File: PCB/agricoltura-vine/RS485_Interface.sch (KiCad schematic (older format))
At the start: 10 parts

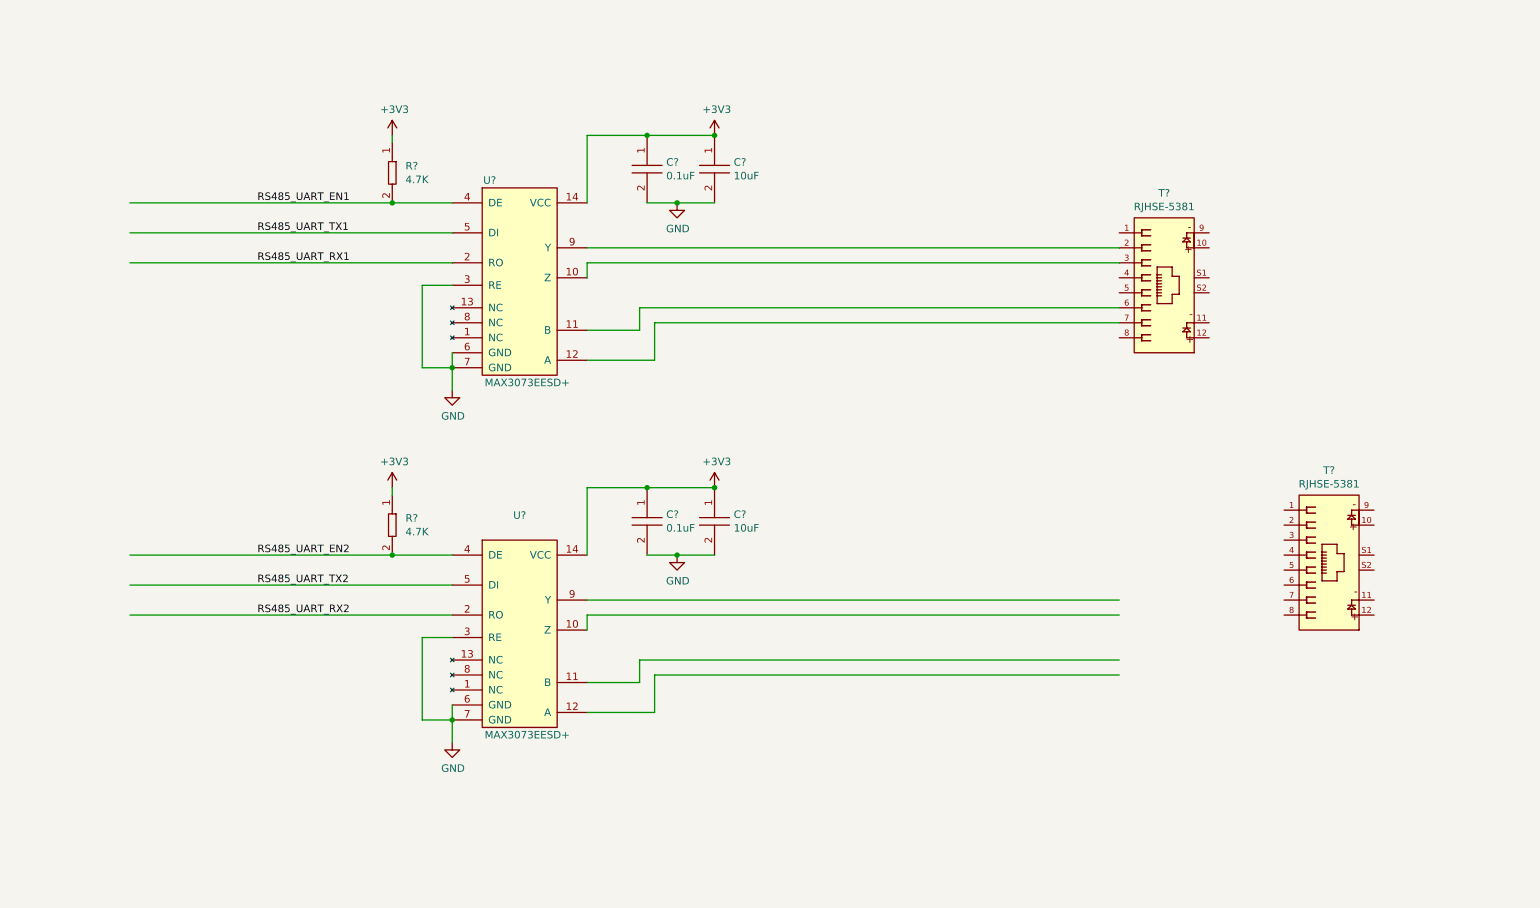
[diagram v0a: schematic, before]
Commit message: Schematic process
scheamtics laid out for all board subsyhstems, connecting MCU to subsystems still in progress, power yet to be designed.
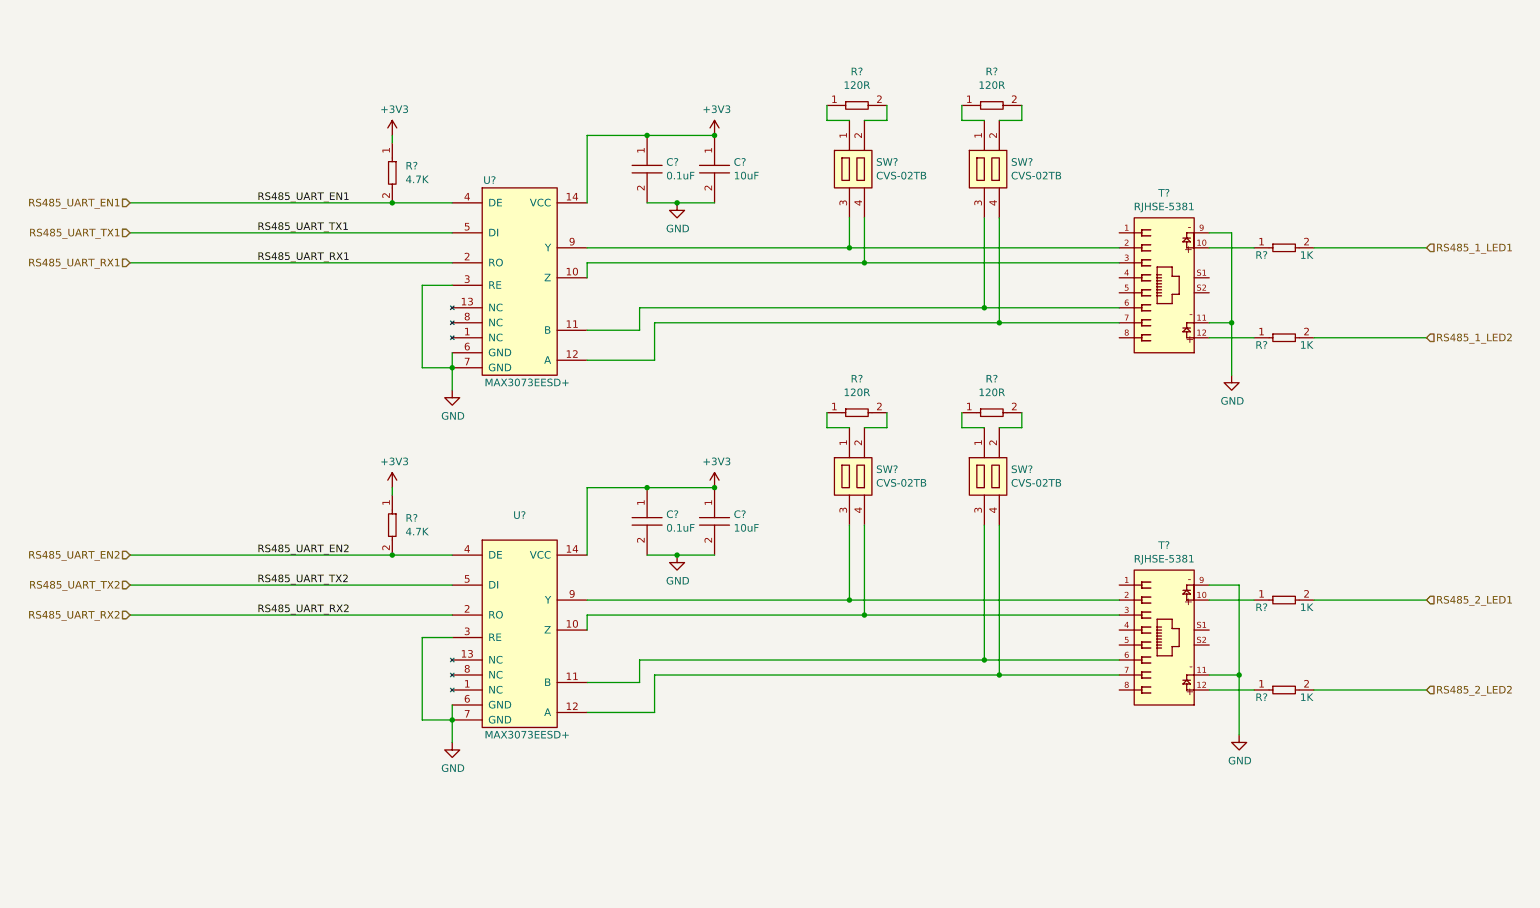
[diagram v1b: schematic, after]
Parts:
- added R? (x4): AC0402FR-07120RL, AVR-KiCAD-Lib-Resistors:R0402, symbol AVR-KiCAD-Lib-Resistors:AC0402FR-07120RL
- added R? (x4): RC0402FR-071KL, AVR-KiCAD-Lib-Resistors:R0402, symbol AVR-KiCAD-Lib-Resistors:RC0402FR-071KL
- added SW? (x4): CVS-02TB, AVR-KiCAD-Lib-Mech-Switches:CVS-02TB, symbol AVR-KiCAD-Lib-Mech-Switches:CVS-02TB
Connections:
- net labels added: RS485_1_LED1, RS485_1_LED2, RS485_2_LED1, RS485_2_LED2
- wire segments 48 -> 96
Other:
- moved on the sheet: T?

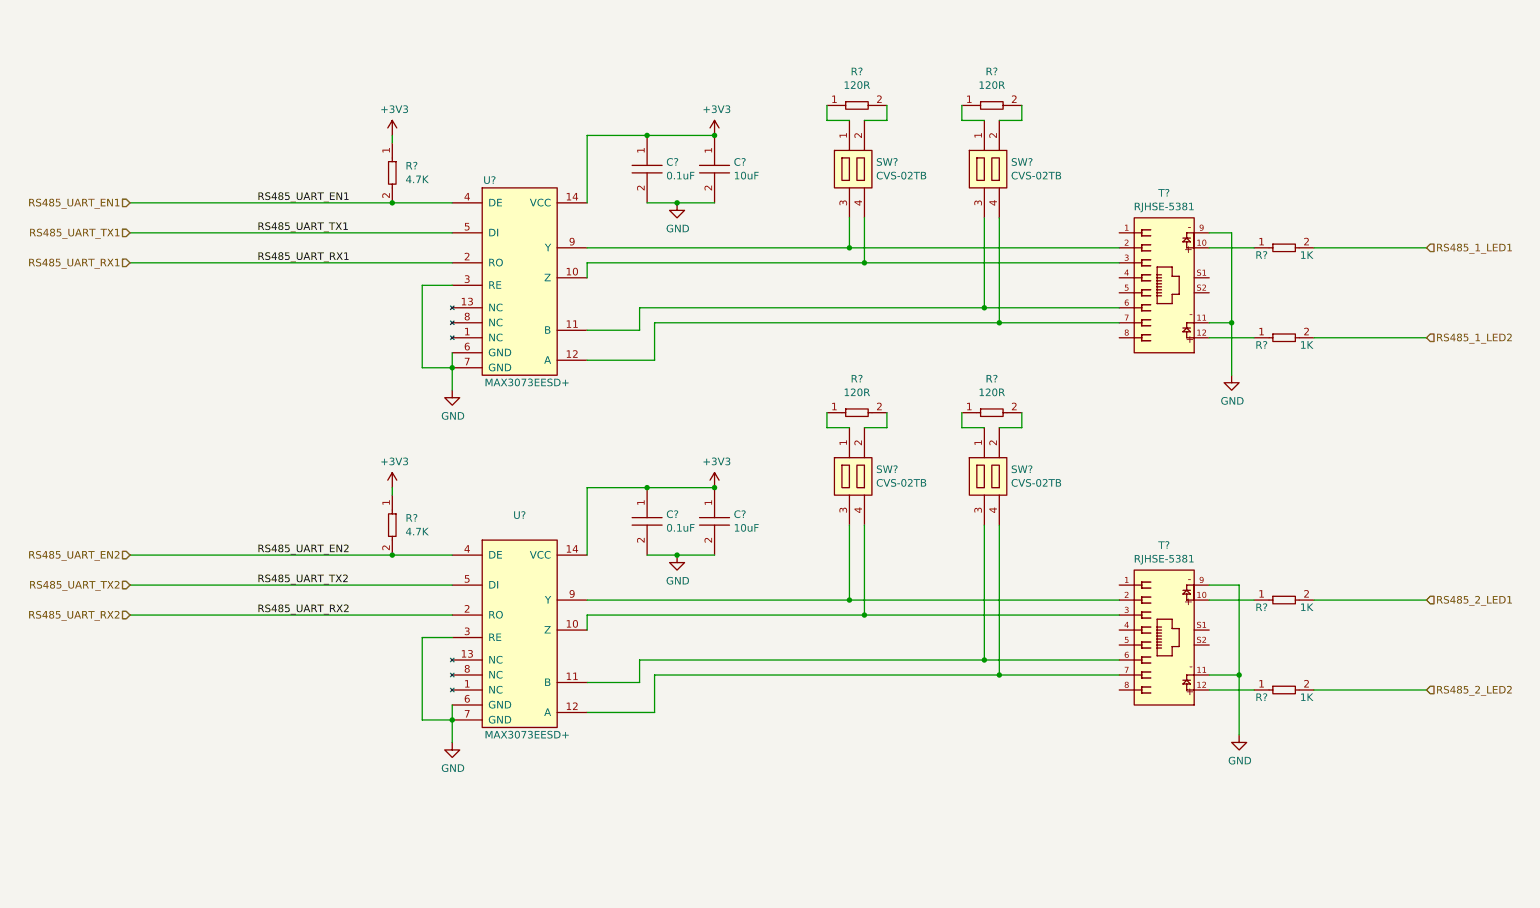
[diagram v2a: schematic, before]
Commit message: Board
Board shape defined, though subject to change. Schematic anotated and parts exported to board.
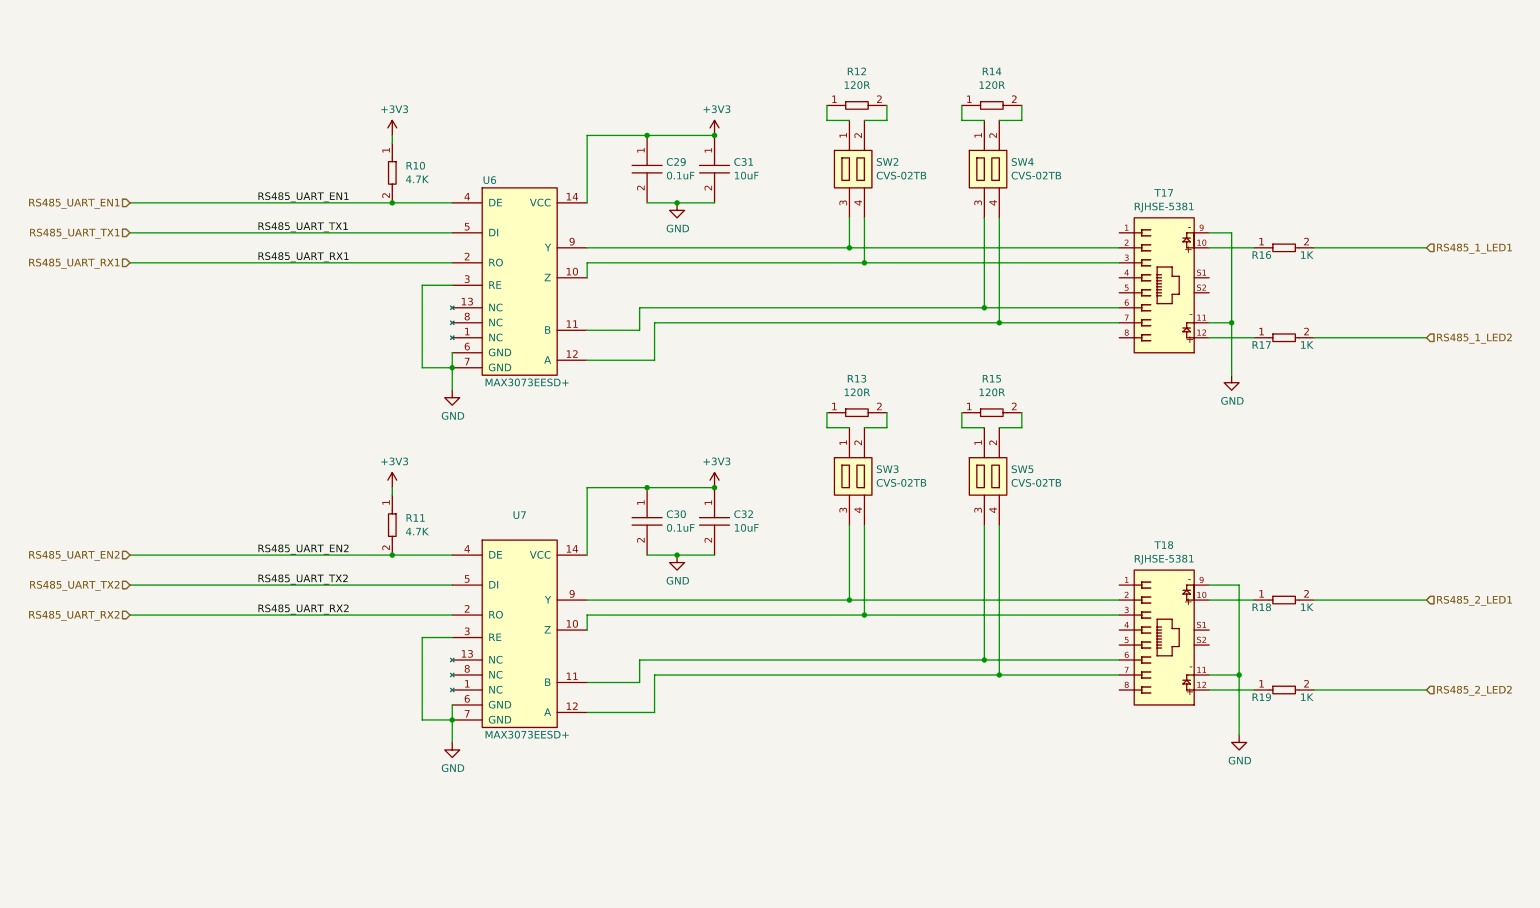
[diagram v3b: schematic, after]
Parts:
- gave numbers to parts that had none: 22
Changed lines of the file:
@@
 $EndDescr
 $Comp
-L AVR-KiCAD-Lib-ICs:MAX3073EESD+ U?
+L AVR-KiCAD-Lib-ICs:MAX3073EESD+ U6
 U 1 1 5EFD4AB7
 P 4300 2150
-F 0 "U?" H 4350 2250 50  0000 C CNN
+F 0 "U6" H 4350 2250 50  0000 C CNN
 F 1 "MAX3073EESD+" H 4350 2350 50  0001 C CNN
 F 2 "AVR-KiCAD-Lib-ICs:MAX3073EESD&plus_" H 4100 2150 50  0001 C CNN
@@
 $EndComp
 $Comp
-L AVR-KiCAD-Lib-ICs:MAX3073EESD+ U?
+L AVR-KiCAD-Lib-ICs:MAX3073EESD+ U7
 U 1 1 5EFD5614
 P 4300 4500
-F 0 "U?" H 4550 4715 50  0000 C CNN
+F 0 "U7" H 4550 4715 50  0000 C CNN
 F 1 "MAX3073EESD+" H 4350 4700 50  0001 C CNN
 F 2 "AVR-KiCAD-Lib-ICs:MAX3073EESD&plus_" H 4100 4500 50  0001 C CNN
@@
 $EndComp
 $Comp
-L AVR-KiCAD-Lib-Connectors:RJHSE-5381 T?
+L AVR-KiCAD-Lib-Connectors:RJHSE-5381 T17
 U 1 1 5EFFC7BA
 P 9050 2300
-F 0 "T?" H 9250 2465 50  0000 C CNN
+F 0 "T17" H 9250 2465 50  0000 C CNN
 F 1 "RJHSE-5381" H 9250 2374 50  0000 C CNN
 F 2 "AVR-KiCAD-Lib-Connectors:AMPHENOL_RJHSE-5381" H 8850 2300 50  0001 C CNN
@@
 $EndComp
 $Comp
-L AVR-KiCAD-Lib-Connectors:RJHSE-5381 T?
+L AVR-KiCAD-Lib-Connectors:RJHSE-5381 T18
 U 1 1 5EFFF009
 P 9050 4650
-F 0 "T?" H 9250 4815 50  0000 C CNN
+F 0 "T18" H 9250 4815 50  0000 C CNN
 F 1 "RJHSE-5381" H 9250 4724 50  0000 C CNN
 F 2 "AVR-KiCAD-Lib-Connectors:AMPHENOL_RJHSE-5381" H 8850 4650 50  0001 C CNN
@@
 	5450 3000 7750 3000
 $Comp
-L power:GND #PWR?
+L power:GND #PWR044
 U 1 1 5F017F66
 P 5600 2200
-F 0 "#PWR?" H 5600 1950 50  0001 C CNN
+F 0 "#PWR044" H 5600 1950 50  0001 C CNN
 F 1 "GND" H 5605 2027 50  0000 C CNN
 F 2 "" H 5600 2200 50  0001 C CNN
@@
 	5600 2200 5850 2200
 $Comp
-L power:GND #PWR?
+L power:GND #PWR042
 U 1 1 5F01B1E0
 P 4100 3450
-F 0 "#PWR?" H 4100 3200 50  0001 C CNN
+F 0 "#PWR042" H 4100 3200 50  0001 C CNN
 F 1 "GND" H 4105 3277 50  0000 C CNN
 F 2 "" H 4100 3450 50  0001 C CNN
@@
 	4100 3300 4100 3450
 $Comp
-L AVR-KiCAD-Lib-Resistors:RC0402FR-074K7L R?
+L AVR-KiCAD-Lib-Resistors:RC0402FR-074K7L R10
 U 1 1 5F01CC10
 P 3700 2000
-F 0 "R?" V 3654 2088 50  0000 L CNN
+F 0 "R10" V 3654 2088 50  0000 L CNN
 F 1 "RC0402FR-074K7L" V 3700 2087 50  0001 L CNN
 F 2 "AVR-KiCAD-Lib-Resistors:R0402" H 3700 2000 50  0001 C CNN
@@
 $EndComp
 $Comp
-L power:+3V3 #PWR?
+L power:+3V3 #PWR040
 U 1 1 5F01FD5B
 P 3700 1750
-F 0 "#PWR?" H 3700 1600 50  0001 C CNN
+F 0 "#PWR040" H 3700 1600 50  0001 C CNN
 F 1 "+3V3" H 3715 1923 50  0000 C CNN
 F 2 "" H 3700 1750 50  0001 C CNN
@@
 	5450 5350 7750 5350
 $Comp
-L AVR-KiCAD-Lib-Capacitors:C0402C104K9PACTU C?
+L AVR-KiCAD-Lib-Capacitors:C0402C104K9PACTU C30
 U 1 1 5F03829B
 P 5400 4300
-F 0 "C?" V 5379 4428 50  0000 L CNN
+F 0 "C30" V 5379 4428 50  0000 L CNN
 F 1 "C0402C104K9PACTU" H 5450 4500 50  0001 C CNN
 F 2 "AVR-KiCAD-Lib-Resistors:R0402" H 5200 4300 50  0001 C CNN
@@
 $EndComp
 $Comp
-L AVR-KiCAD-Lib-Capacitors:GRM188R61A106KE69J C?
+L AVR-KiCAD-Lib-Capacitors:GRM188R61A106KE69J C32
 U 1 1 5F0382BA
 P 5850 4300
-F 0 "C?" V 5829 4428 50  0000 L CNN
+F 0 "C32" V 5829 4428 50  0000 L CNN
 F 1 "GRM188R61A106KE69J" H 5900 4500 50  0001 C CNN
 F 2 "AVR-KiCAD-Lib-Capacitors:C0603" H 5650 4300 50  0001 C CNN
@@
 $EndComp
 $Comp
-L power:GND #PWR?
+L power:GND #PWR045
 U 1 1 5F0382C0
 P 5600 4550
-F 0 "#PWR?" H 5600 4300 50  0001 C CNN
+F 0 "#PWR045" H 5600 4300 50  0001 C CNN
 F 1 "GND" H 5605 4377 50  0000 C CNN
 F 2 "" H 5600 4550 50  0001 C CNN
@@
 	5600 4550 5850 4550
 $Comp
-L power:+3V3 #PWR?
+L power:+3V3 #PWR047
 U 1 1 5F0382CD
 P 5850 4100
-F 0 "#PWR?" H 5850 3950 50  0001 C CNN
+F 0 "#PWR047" H 5850 3950 50  0001 C CNN
 F 1 "+3V3" H 5865 4273 50  0000 C CNN
 F 2 "" H 5850 4100 50  0001 C CNN
@@
 Connection ~ 5850 4100
 $Comp
-L power:GND #PWR?
+L power:GND #PWR043
 U 1 1 5F0382D4
 P 4100 5800
-F 0 "#PWR?" H 4100 5550 50  0001 C CNN
+F 0 "#PWR043" H 4100 5550 50  0001 C CNN
 F 1 "GND" H 4105 5627 50  0000 C CNN
 F 2 "" H 4100 5800 50  0001 C CNN
@@
 	4100 5650 4100 5800
 $Comp
-L AVR-KiCAD-Lib-Resistors:RC0402FR-074K7L R?
+L AVR-KiCAD-Lib-Resistors:RC0402FR-074K7L R11
 U 1 1 5F0382F6
 P 3700 4350
-F 0 "R?" V 3654 4438 50  0000 L CNN
+F 0 "R11" V 3654 4438 50  0000 L CNN
 F 1 "RC0402FR-074K7L" V 3700 4437 50  0001 L CNN
 F 2 "AVR-KiCAD-Lib-Resistors:R0402" H 3700 4350 50  0001 C CNN
@@
 $EndComp
 $Comp
-L power:+3V3 #PWR?
+L power:+3V3 #PWR041
 U 1 1 5F0382FC
 P 3700 4100
-F 0 "#PWR?" H 3700 3950 50  0001 C CNN
+F 0 "#PWR041" H 3700 3950 50  0001 C CNN
 F 1 "+3V3" H 3715 4273 50  0000 C CNN
 F 2 "" H 3700 4100 50  0001 C CNN
@@
 RS485_UART_EN2
 $Comp
-L AVR-KiCAD-Lib-Resistors:AC0402FR-07120RL R?
+L AVR-KiCAD-Lib-Resistors:AC0402FR-07120RL R12
 U 1 1 5F099D8E
 P 6800 1550
-F 0 "R?" H 6800 1775 50  0000 C CNN
+F 0 "R12" H 6800 1775 50  0000 C CNN
 F 1 "AC0402FR-07120RL" H 6800 1775 50  0001 C CNN
 F 2 "AVR-KiCAD-Lib-Resistors:R0402" H 6800 1550 50  0001 C CNN
@@
 $EndComp
 $Comp
-L AVR-KiCAD-Lib-Mech-Switches:CVS-02TB SW?
+L AVR-KiCAD-Lib-Mech-Switches:CVS-02TB SW2
 U 1 1 5F09CD45
 P 6700 1900
-F 0 "SW?" H 6928 1871 50  0000 L CNN
+F 0 "SW2" H 6928 1871 50  0000 L CNN
 F 1 "CVS-02TB" H 6928 1780 50  0000 L CNN
 F 2 "AVR-KiCAD-Lib-Mech-Switches:CVS-02TB" H 6700 2400 50  0001 C CNN
@@
 	6850 2600 5000 2600
 $Comp
-L AVR-KiCAD-Lib-Resistors:AC0402FR-07120RL R?
+L AVR-KiCAD-Lib-Resistors:AC0402FR-07120RL R14
 U 1 1 5F0B259F
 P 7700 1550
-F 0 "R?" H 7700 1775 50  0000 C CNN
+F 0 "R14" H 7700 1775 50  0000 C CNN
 F 1 "AC0402FR-07120RL" H 7700 1775 50  0001 C CNN
 F 2 "AVR-KiCAD-Lib-Resistors:R0402" H 7700 1550 50  0001 C CNN
@@
 $EndComp
 $Comp
-L AVR-KiCAD-Lib-Mech-Switches:CVS-02TB SW?
+L AVR-KiCAD-Lib-Mech-Switches:CVS-02TB SW4
 U 1 1 5F0B25BE
 P 7600 1900
-F 0 "SW?" H 7828 1871 50  0000 L CNN
+F 0 "SW4" H 7828 1871 50  0000 L CNN
 F 1 "CVS-02TB" H 7828 1780 50  0000 L CNN
 F 2 "AVR-KiCAD-Lib-Mech-Switches:CVS-02TB" H 7600 2400 50  0001 C CNN
@@
 	7750 3000 8550 3000
 $Comp
-L AVR-KiCAD-Lib-Resistors:AC0402FR-07120RL R?
+L AVR-KiCAD-Lib-Resistors:AC0402FR-07120RL R13
 U 1 1 5F0B9FE5
 P 6800 3600
-F 0 "R?" H 6800 3825 50  0000 C CNN
+F 0 "R13" H 6800 3825 50  0000 C CNN
 F 1 "AC0402FR-07120RL" H 6800 3825 50  0001 C CNN
 F 2 "AVR-KiCAD-Lib-Resistors:R0402" H 6800 3600 50  0001 C CNN
@@
 $EndComp
 $Comp
-L AVR-KiCAD-Lib-Mech-Switches:CVS-02TB SW?
+L AVR-KiCAD-Lib-Mech-Switches:CVS-02TB SW3
 U 1 1 5F0BA004
 P 6700 3950
-F 0 "SW?" H 6928 3921 50  0000 L CNN
+F 0 "SW3" H 6928 3921 50  0000 L CNN
 F 1 "CVS-02TB" H 6928 3830 50  0000 L CNN
 F 2 "AVR-KiCAD-Lib-Mech-Switches:CVS-02TB" H 6700 4450 50  0001 C CNN
@@
 	7000 3700 7000 3600
 $Comp
-L AVR-KiCAD-Lib-Resistors:AC0402FR-07120RL R?
+L AVR-KiCAD-Lib-Resistors:AC0402FR-07120RL R15
 U 1 1 5F0BA027
 P 7700 3600
-F 0 "R?" H 7700 3825 50  0000 C CNN
+F 0 "R15" H 7700 3825 50  0000 C CNN
 F 1 "AC0402FR-07120RL" H 7700 3825 50  0001 C CNN
 F 2 "AVR-KiCAD-Lib-Resistors:R0402" H 7700 3600 50  0001 C CNN
@@
 $EndComp
 $Comp
-L AVR-KiCAD-Lib-Mech-Switches:CVS-02TB SW?
+L AVR-KiCAD-Lib-Mech-Switches:CVS-02TB SW5
 U 1 1 5F0BA046
 P 7600 3950
-F 0 "SW?" H 7828 3921 50  0000 L CNN
+F 0 "SW5" H 7828 3921 50  0000 L CNN
 F 1 "CVS-02TB" H 7828 3830 50  0000 L CNN
 F 2 "AVR-KiCAD-Lib-Mech-Switches:CVS-02TB" H 7600 4450 50  0001 C CNN
@@
 	7750 5350 8550 5350
 $Comp
-L AVR-KiCAD-Lib-Resistors:RC0402FR-071KL R?
+L AVR-KiCAD-Lib-Resistors:RC0402FR-071KL R16
 U 1 1 5F0C6C33
 P 9650 2500
-F 0 "R?" H 9500 2450 50  0000 C CNN
+F 0 "R16" H 9500 2450 50  0000 C CNN
 F 1 "RC0402FR-071KL" H 9650 2725 50  0001 C CNN
 F 2 "AVR-KiCAD-Lib-Resistors:R0402" H 9650 2500 50  0001 C CNN
@@
 $EndComp
 $Comp
-L AVR-KiCAD-Lib-Resistors:RC0402FR-071KL R?
+L AVR-KiCAD-Lib-Resistors:RC0402FR-071KL R17
 U 1 1 5F0C79C2
 P 9650 3100
-F 0 "R?" H 9500 3050 50  0000 C CNN
+F 0 "R17" H 9500 3050 50  0000 C CNN
 F 1 "RC0402FR-071KL" H 9650 3325 50  0001 C CNN
 F 2 "AVR-KiCAD-Lib-Resistors:R0402" H 9650 3100 50  0001 C CNN
@@
 $EndComp
 $Comp
-L AVR-KiCAD-Lib-Resistors:RC0402FR-071KL R?
+L AVR-KiCAD-Lib-Resistors:RC0402FR-071KL R18
 U 1 1 5F0CC945
 P 9650 4850
-F 0 "R?" H 9500 4800 50  0000 C CNN
+F 0 "R18" H 9500 4800 50  0000 C CNN
 F 1 "RC0402FR-071KL" H 9650 5075 50  0001 C CNN
 F 2 "AVR-KiCAD-Lib-Resistors:R0402" H 9650 4850 50  0001 C CNN
@@
 $EndComp
 $Comp
-L AVR-KiCAD-Lib-Resistors:RC0402FR-071KL R?
+L AVR-KiCAD-Lib-Resistors:RC0402FR-071KL R19
 U 1 1 5F0CC964
 P 9650 5450
-F 0 "R?" H 9500 5400 50  0000 C CNN
+F 0 "R19" H 9500 5400 50  0000 C CNN
 F 1 "RC0402FR-071KL" H 9650 5675 50  0001 C CNN
 F 2 "AVR-KiCAD-Lib-Resistors:R0402" H 9650 5450 50  0001 C CNN
@@
 Connection ~ 9300 3000
 $Comp
-L power:GND #PWR?
+L power:GND #PWR048
 U 1 1 5F0DA94B
 P 9300 3350
-F 0 "#PWR?" H 9300 3100 50  0001 C CNN
+F 0 "#PWR048" H 9300 3100 50  0001 C CNN
 F 1 "GND" H 9305 3177 50  0000 C CNN
 F 2 "" H 9300 3350 50  0001 C CNN
@@
 Connection ~ 9350 5350
 $Comp
-L power:GND #PWR?
+L power:GND #PWR049
 U 1 1 5F0DF7B7
 P 9350 5750
-F 0 "#PWR?" H 9350 5500 50  0001 C CNN
+F 0 "#PWR049" H 9350 5500 50  0001 C CNN
 F 1 "GND" H 9355 5577 50  0000 C CNN
 F 2 "" H 9350 5750 50  0001 C CNN
@@
 Connection ~ 5850 1750
 $Comp
-L power:+3V3 #PWR?
+L power:+3V3 #PWR046
 U 1 1 5F01A2C3
 P 5850 1750
-F 0 "#PWR?" H 5850 1600 50  0001 C CNN
+F 0 "#PWR046" H 5850 1600 50  0001 C CNN
 F 1 "+3V3" H 5865 1923 50  0000 C CNN
 F 2 "" H 5850 1750 50  0001 C CNN
@@
 	5850 1750 5400 1750
 $Comp
-L AVR-KiCAD-Lib-Capacitors:GRM188R61A106KE69J C?
+L AVR-KiCAD-Lib-Capacitors:GRM188R61A106KE69J C31
 U 1 1 5F015F3F
 P 5850 1950
-F 0 "C?" V 5829 2078 50  0000 L CNN
+F 0 "C31" V 5829 2078 50  0000 L CNN
 F 1 "GRM188R61A106KE69J" H 5900 2150 50  0001 C CNN
 F 2 "AVR-KiCAD-Lib-Capacitors:C0603" H 5650 1950 50  0001 C CNN
@@
 $EndComp
 $Comp
-L AVR-KiCAD-Lib-Capacitors:C0402C104K9PACTU C?
+L AVR-KiCAD-Lib-Capacitors:C0402C104K9PACTU C29
 U 1 1 5F01065A
 P 5400 1950
-F 0 "C?" V 5379 2078 50  0000 L CNN
+F 0 "C29" V 5379 2078 50  0000 L CNN
 F 1 "C0402C104K9PACTU" H 5450 2150 50  0001 C CNN
 F 2 "AVR-KiCAD-Lib-Resistors:R0402" H 5200 1950 50  0001 C CNN
